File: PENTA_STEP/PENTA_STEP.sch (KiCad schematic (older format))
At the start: 159 parts, among them J1 DB25_Female_LCNC, J10 ENC_HEADER, J11 ENC_HEADER, J12 PSoC_PROG, J13 PWR_SW_CH1, J14 SCREW TERM, J15 SCREW TERM, J16 ENC_HEADER, J17 ENC_HEADER, J18 SCREW TERM, J19 SCREW TERM, J2 MTA-100, J20 CYP_I2C, J21 PWR_SW_CH2, J3 USB_B, J4 SPARE_IN, J5 ENC_HEADER, J6 Conn_02x02_Odd_Even, J7 CYP_GPIO, J8 ICSP, J9 SCREW TERM, Q21 AON7804, U1 ATTINY841-SSU, U2 CY8C5468AXI-LP106, Y1 10MHz

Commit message: majority routed, eliminated ATTINY coprocessor
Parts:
- removed C1: 10u, Capacitor_SMD:C_0603_1608Metric_Pad1.05x0.95mm_HandSolder, symbol Device:C
- removed C2: 100n, Capacitor_SMD:C_0603_1608Metric_Pad1.05x0.95mm_HandSolder, symbol Device:C
- removed C5, C7: 18p, Capacitor_SMD:C_0603_1608Metric_Pad1.05x0.95mm_HandSolder, symbol Device:C
- removed J6: Conn_02x02_Odd_Even, Connector_PinHeader_2.54mm:PinHeader_2x02_P2.54mm_Vertical, symbol Connector_Generic:Conn_02x02_Odd_Even
- removed J8: ICSP, Connector_PinHeader_2.54mm:PinHeader_2x03_P2.54mm_Vertical, symbol CUSTOM:ICSP
- removed JP10, JP2, JP21, JP23, JP25, JP27, JP29, JP4, JP40, JP42, JP44, JP46, JP48, JP50, JP52, JP54, JP56, JP59, JP6, JP8, JP81, JP83, JP85, JP87, JP89, JP99: SolderJumper_2_Open, CUSTOM_FP:small_triangle_jumper, symbol Jumper:SolderJumper_2_Open
- removed R5: 10k, Resistor_SMD:R_0603_1608Metric_Pad1.05x0.95mm_HandSolder, symbol Device:R
- removed U1: ATTINY841-SSU, CUSTOM_FP:ATTINY841-SSU, symbol 2019-12-26_17-57-50:ATTINY841-SSU
- removed Y1: 10MHz, CUSTOM_FP:CX5032GB10000H0PESZZ, symbol Device:Crystal
- added NT1: Net-Tie_2, symbol Device:Net-Tie_2
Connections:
- net CYP_CS1: now also U2.19 (P53); no longer U2.9 (P67)
- net CYP_CS2: now also U2.2 (P26); no longer U2.98 (P23)
- net CYP_CS3: now also U2.90 (P61); no longer U2.97 (P22)
- net CYP_CS4: now also U2.78 (P06); no longer U2.96 (P21)
- net CYP_CS5: now also U2.68 (P123); no longer U2.95 (P20)
- net CYP_DIR1: now also U2.8 (P66); no longer U2.7 (P65)
- net CYP_DIR2: now also U2.96 (P21); no longer U2.79 (P07)
- net CYP_DIR3: now also U2.82 (P44); no longer U2.73 (P02)
- net CYP_DIR4: now also U2.72 (P01); no longer U2.52 (P37)
- net CYP_DIR5: now also U2.53 (P120); no longer U2.46 (P32)
- net CYP_STEP1: now also U2.9 (P67); no longer U2.8 (P66)
- net CYP_STEP2: now also U2.97 (P22); no longer U2.80 (P42)
- net CYP_STEP3: now also U2.83 (P45); no longer U2.74 (P03)
- net CYP_STEP4: now also U2.73 (P02); no longer U2.69 (P40)
- net CYP_STEP5: now also U2.54 (P121); no longer U2.47 (P33)
- net DIAG_0_1: now also U2.6 (P64); no longer U2.83 (P45)
- net DIAG_0_2: now also U2.94 (P155); no longer U2.78 (P06)
- net DIAG_0_3: now also U2.80 (P42); no longer U2.72 (P01)
- net DIAG_0_4: now also U2.71 (P00); no longer U2.51 (P36)
- net DIAG_0_5: now also U2.52 (P37); no longer U2.45 (P31)
- net DIAG_1_1: now also U2.3 (P27); no longer U2.82 (P44)
- net DIAG_1_2: now also U2.93 (P154); no longer U2.77 (P05)
- net DIAG_1_3: now also U2.79 (P07); no longer U2.71 (P00)
- net DIAG_1_4: now also U2.70 (P41); no longer U2.49 (P35)
- net DIAG_1_5: now also U2.51 (P36); no longer U2.44 (P30)
- net PWR_SW_CH1: now also U2.92 (P63); no longer U2.85 (P47)
- net PWR_SW_CH2: now also U2.91 (P62); no longer U2.84 (P46)
- net VCC_CONT: now also JP77.1 (A), JP78.1 (A), JP79.1 (A), NT1.2
- net VTARG: now also NT1.1
- net ~CYP_ENA_1: now also U2.7 (P65); no longer U2.89 (P60)
- net ~CYP_ENA_2: now also U2.95 (P20); no longer U2.81 (P43)
- net ~CYP_ENA_3: now also U2.81 (P43); no longer U2.76 (P04)
- net ~CYP_ENA_4: now also U2.69 (P40); no longer U2.70 (P41)
- net ~CYP_ENA_5: now also U2.49 (P35); no longer U2.48 (P34)
- net CYP_SCK2: now reaches U2.1 (P25)
- net CYP_SCK2: now also JP20.1 (A)
- net CYP_MISO1: now reaches U2.16 (P50)
- net CYP_MISO1: now also JP7.1 (A)
- net CYP_MOSI1: now reaches U2.17 (P51)
- net CYP_MOSI1: now also JP5.1 (A)
- net CYP_SCK1: now reaches U2.18 (P52)
- net CYP_SCK1: now also JP1.1 (A)
- net CYP_MISO5: now reaches U2.55 (P152)
- net CYP_MISO5: now also JP86.1 (A)
- net CYP_MOSI5: now reaches U2.56 (P153)
- net CYP_MOSI5: now also JP84.1 (A)
- net CYP_SCK5: now reaches U2.67 (P122)
- net CYP_SCK5: now also JP80.1 (A)
- net CYP_MOSI2: now reaches U2.99 (P24)
- net CYP_MOSI2: now also JP24.1 (A)
- removed net CYP_MISO: JP26.1 (A), JP45.1 (A), JP53.1 (A), JP7.1 (A), JP86.1 (A), U2.90 (P61)
- removed net CYP_MOSI: JP24.1 (A), JP43.1 (A), JP5.1 (A), JP51.1 (A), JP84.1 (A), U2.91 (P62)
- removed net CYP_SCK: JP1.1 (A), JP20.1 (A), JP39.1 (A), JP47.1 (A), JP80.1 (A), U2.92 (P63)
- new net CYP_MISO2: JP26.1 (A), U2.98 (P23)
- new net CYP_MISO3: JP45.1 (A), U2.84 (P46)
- new net CYP_MISO4: JP53.1 (A), U2.74 (P03)
- new net CYP_MOSI3: JP43.1 (A), U2.85 (P47)
- new net CYP_MOSI4: JP51.1 (A), U2.76 (P04)
- new net CYP_SCK3: JP39.1 (A), U2.89 (P60)
- new net CYP_SCK4: JP47.1 (A), U2.77 (P05)
- no-connect marks 22 -> 10

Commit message: completed preliminary routing, still need plane touchup
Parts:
- removed NT1: Net-Tie_2, symbol Device:Net-Tie_2
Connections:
- net VTARG is gone; now on net VCC_CONT: J12.4 (Pin_4)
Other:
- note added: "C++ on PSoC: https://blog.mbedded.ninja/programming/microcontrollers/psoc/using-cplusplus-with-psoc-creator/\n\nBOM tool\nhttps://github.com/SchrodingersGat/KiBoM\n\nConsider freewheeling diode protection for motor pins like this:\nhttps://github.com/watterott/SilentStepStick/blob/master/hardware/StepStick-Protector_v20.pdf\nBut using THT diodes (due to lack of space, these can be soldered under 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"
- note removed: "Notes:\n3x SPI\n4x CS lines minimum\n4X DRV_ENN\n8x DIAG ports (consider using I2C I/O expander such as TCA9554DBR. This has interrupt capabilities. 2x for I2C, 1x for interrupt)\n4x STEP\n4x DIR\n\n22 total\n\n\nATMEGA 32u4\nhttps://www.digikey.com/product-detail/en/microchip-technology/ATMEGA32U4RC-AU/ATMEGA32U4RC-AU-ND/2507982\n\nPSoC 4 may be a much better/cheaper alternative. https://www.you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"
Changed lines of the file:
@@
 	-1   0    0    1
 $EndComp
-Text Notes 14000 14400 0    79   ~ 16
-Notes:\n3x SPI\n4x CS lines minimum\n4X DRV_ENN\n8x DIAG ports (consider using I2C I/O expander such as  TCA9554DBR. This has interrupt  capabilities. 2x for I2C, 1x for interrupt)\n4x STEP\n4x DIR\n\n22 total\n\n\nATMEGA 32u4\nhttps://www.digikey.com/product-detail/en/microchip-technology/ATMEGA32U4RC-AU/ATMEGA32U4RC-AU-ND/2507982\n\nPSoC 4 may be a much better/cheaper alternative. https://www.youtube.com/watch?v=cHqENmk5RLE\nC++ on PSoC: https://blog.mbedded.ninja/programming/microcontrollers/psoc/using-cplusplus-with-psoc-creator/\nhttps://www.digikey.com/product-detail/en/cypress-semiconductor-corp/CY8C5468AXI-LP106/2015-CY8C5468AXI-LP106-ND/9809570\n\nUse ATTINY as the startup and go option, with a feature rich PSoC parallel processor\n\nBOM tool\nhttps://github.com/SchrodingersGat/KiBoM
+Text Notes 13750 12750 0    79   ~ 16
+C++ on PSoC: https://blog.mbedded.ninja/programming/microcontrollers/psoc/using-cplusplus-with-psoc-creator/\n\nBOM tool\nhttps://github.com/SchrodingersGat/KiBoM\n\nConsider freewheeling diode protection for motor pins like this:\nhttps://github.com/watterott/SilentStepStick/blob/master/hardware/StepStick-Protector_v20.pdf\nBut using THT diodes (due to lack of space, these can be soldered under the board OR inserted into the screw terminals):\nhttps://www.digikey.com/product-detail/en/smc-diode-solutions/SB5100TA/1655-1524-1-ND/6022969
 Text Label 11050 5200 0    50   ~ 0
 ~PAR_ENA
@@
 	1    0    0    -1
 $EndComp
-Text Label 12250 12100 2    50   ~ 0
+Text Label 12300 12100 2    50   ~ 0
 RST
 $Comp
@@
 $EndComp
 Wire Wire Line
-	11950 12100 12250 12100
+	11950 12100 12300 12100
 Wire Wire Line
-	12250 12000 11950 12000
+	12300 12000 11950 12000
 Wire Wire Line
-	11950 11900 12250 11900
+	11950 11900 12300 11900
 Text Label 10200 13250 2    50   ~ 0
 SWDIO
@@
 	8950 15150 8950 15100
 NoConn ~ 9100 15100
-Text Label 2950 11000 0    50   ~ 0
-VTARG
 Connection ~ 4300 11100
-Wire Wire Line
-	3800 11000 4300 11000
-Wire Wire Line
-	4300 11000 4300 11100
-Wire Wire Line
-	3600 11000 2950 11000
 Text Label 10200 13950 2    50   ~ 0
 ~CYP_ENA_1
@@
 	0    1    1    0
 $EndComp
-Text Label 12250 12000 2    50   ~ 0
+Text Label 12300 12000 2    50   ~ 0
 SWDIO
-Text Label 12250 11900 2    50   ~ 0
+Text Label 12300 11900 2    50   ~ 0
 SWDCLK
-Text Label 12250 12200 2    50   ~ 0
-VTARG
 Wire Wire Line
-	11950 12200 12250 12200
+	11950 12200 12300 12200
 $Sheet
 S 14350 8000 1100 1700
@@
 Wire Wire Line
 	12850 8800 14350 8800
-$Comp
-L Device:Net-Tie_2 NT1
-U 1 1 5F1DA2AE
-P 3700 11000
-F 0 "NT1" H 3700 11178 50  0000 C CNN
-F 1 "Net-Tie_2" H 3700 11087 50  0000 C CNN
-F 2 "" H 3700 11000 50  0001 C CNN
-F 3 "~" H 3700 11000 50  0001 C CNN
-	1    3700 11000
-	1    0    0    -1
-$EndComp
 Wire Wire Line
 	2950 11100 4300 11100
+Text Label 12300 12200 2    50   ~ 0
+VCC_CONT
 $EndSCHEMATC

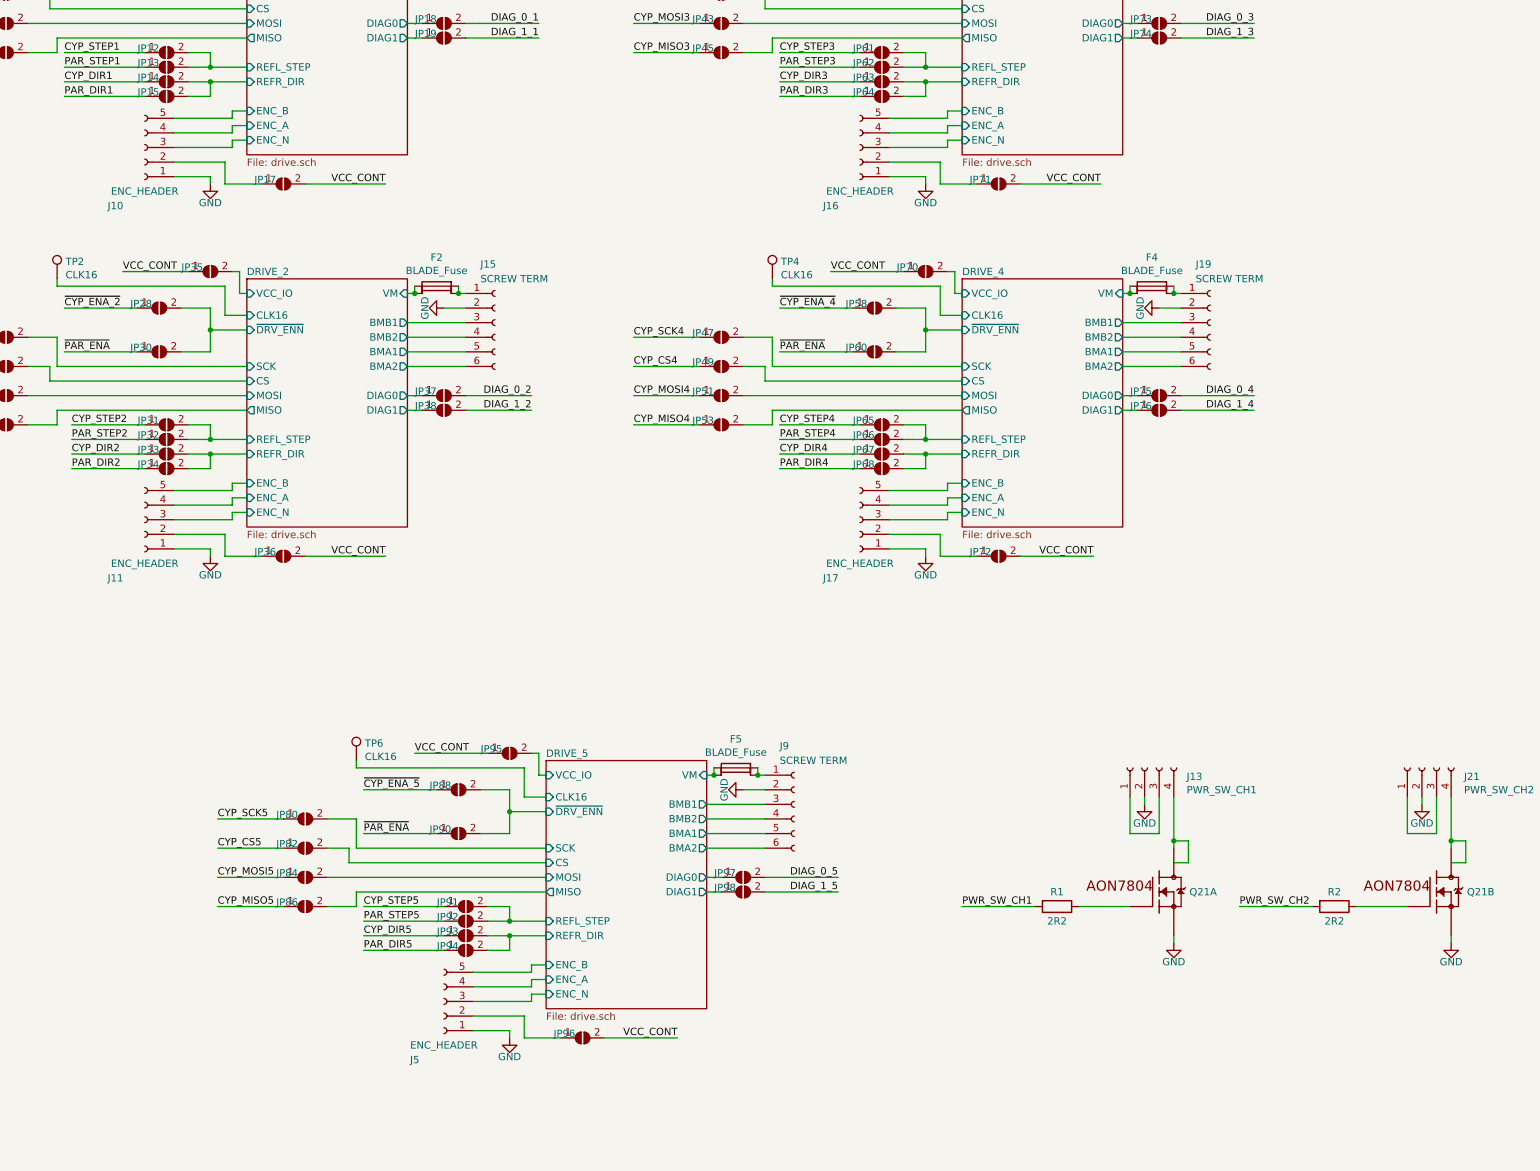
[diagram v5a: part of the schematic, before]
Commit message: finished layout, added top and bottom layer ground pours, added fuses for FET outputs
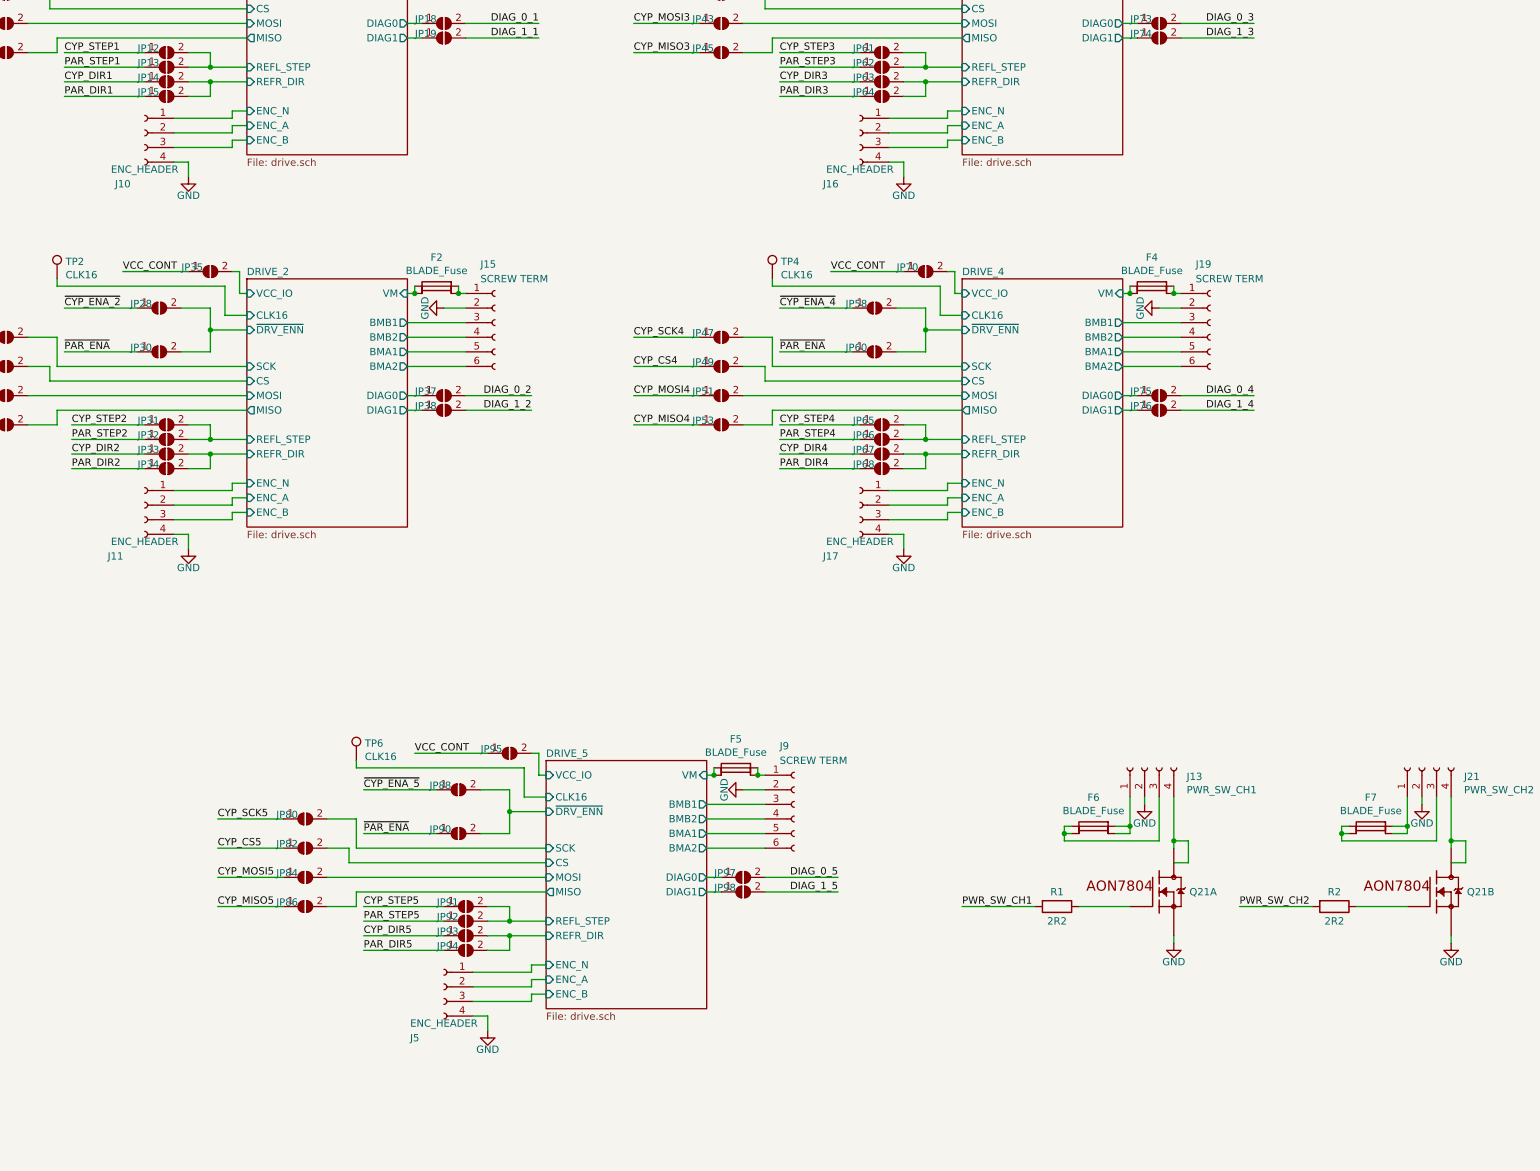
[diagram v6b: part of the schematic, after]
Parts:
- removed J10, J11, J16, J17, J5: ENC_HEADER, Connector_PinHeader_2.54mm:PinHeader_1x05_P2.54mm_Vertical, symbol Connector:Conn_01x05_Female
- removed JP17, JP36, JP71, JP72, JP96: SolderJumper_2_Open, CUSTOM_FP:small_triangle_jumper, symbol Jumper:SolderJumper_2_Open
- added F6, F7: BLADE_Fuse, CUSTOM_FP:keystone_3568_10_fuseholder_THT, symbol CUSTOM:BLADE_Fuse
- added J10, J11, J16, J17, J5: ENC_HEADER, Connector_PinHeader_1.00mm:PinHeader_1x04_P1.00mm_Vertical, symbol Connector:Conn_01x04_Female
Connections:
- net DRIVE_1/ENC_A: now also J10.2 (Pin_2)
- net DRIVE_1/ENC_B: now also J10.3 (Pin_3)
- net DRIVE_1/ENC_N: now also J10.1 (Pin_1)
- net DRIVE_2/ENC_A: now also J11.2 (Pin_2)
- net DRIVE_2/ENC_B: now also J11.3 (Pin_3)
- net DRIVE_2/ENC_N: now also J11.1 (Pin_1)
- net DRIVE_3/ENC_A: now also J16.2 (Pin_2)
- net DRIVE_3/ENC_B: now also J16.3 (Pin_3)
- net DRIVE_3/ENC_N: now also J16.1 (Pin_1)
- net DRIVE_4/ENC_A: now also J17.2 (Pin_2)
- net DRIVE_4/ENC_B: now also J17.3 (Pin_3)
- net DRIVE_4/ENC_N: now also J17.1 (Pin_1)
- net DRIVE_5/ENC_A: now also J5.2 (Pin_2)
- net DRIVE_5/ENC_B: now also J5.3 (Pin_3)
- net DRIVE_5/ENC_N: now also J5.1 (Pin_1)
- net GND: now also J10.4 (Pin_4), J11.4 (Pin_4), J16.4 (Pin_4), J17.4 (Pin_4), J5.4 (Pin_4)
- net at J13.1 (Pin_1): now also F6.3, F6.4; no longer J13.3 (Pin_3)
- net at J21.1 (Pin_1): now also F7.3, F7.4; no longer J21.3 (Pin_3)
- new net: F6.1, F6.2, J13.3 (Pin_3)
- new net: F7.1, F7.2, J21.3 (Pin_3)
